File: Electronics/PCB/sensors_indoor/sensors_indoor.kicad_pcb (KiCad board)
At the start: 4 copper layers, 50 x 50 mm, 61 parts, among them J1 USB4125-GF-A, J2 STDC14, J3 B5B-ZR, Q1 DMN62D0U, SW1 SW_Push, U1 MIC5219-3.3YM5, U10 SPS30, U11 74LVC1G08, U2 STM32WBA5MMG, U3 FM24CL16B, U4 LPS22DF, U5 SHT45-AD1F, U6 SCD41-D-R2, U7 SGP41, U8 OPT4001DTSR, U9 TSOP38436

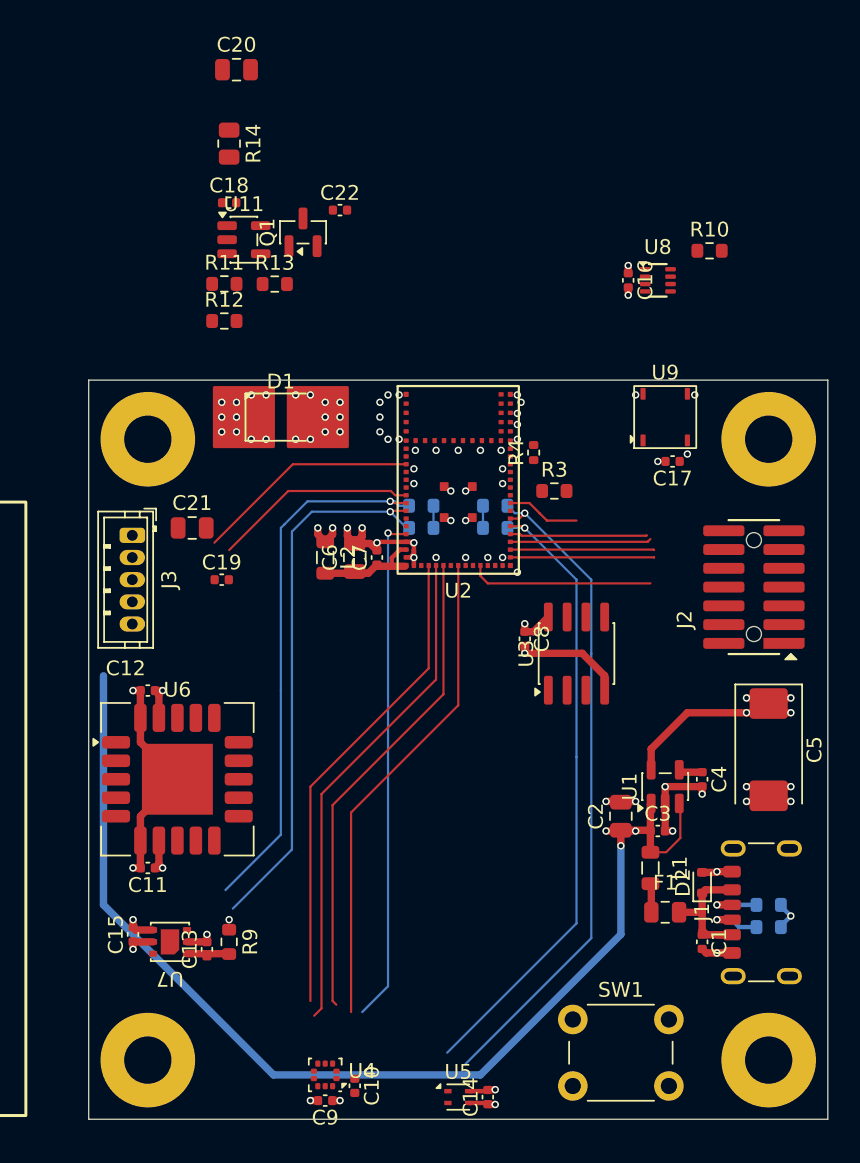
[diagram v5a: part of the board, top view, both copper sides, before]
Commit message: Completed schematic, done most routing
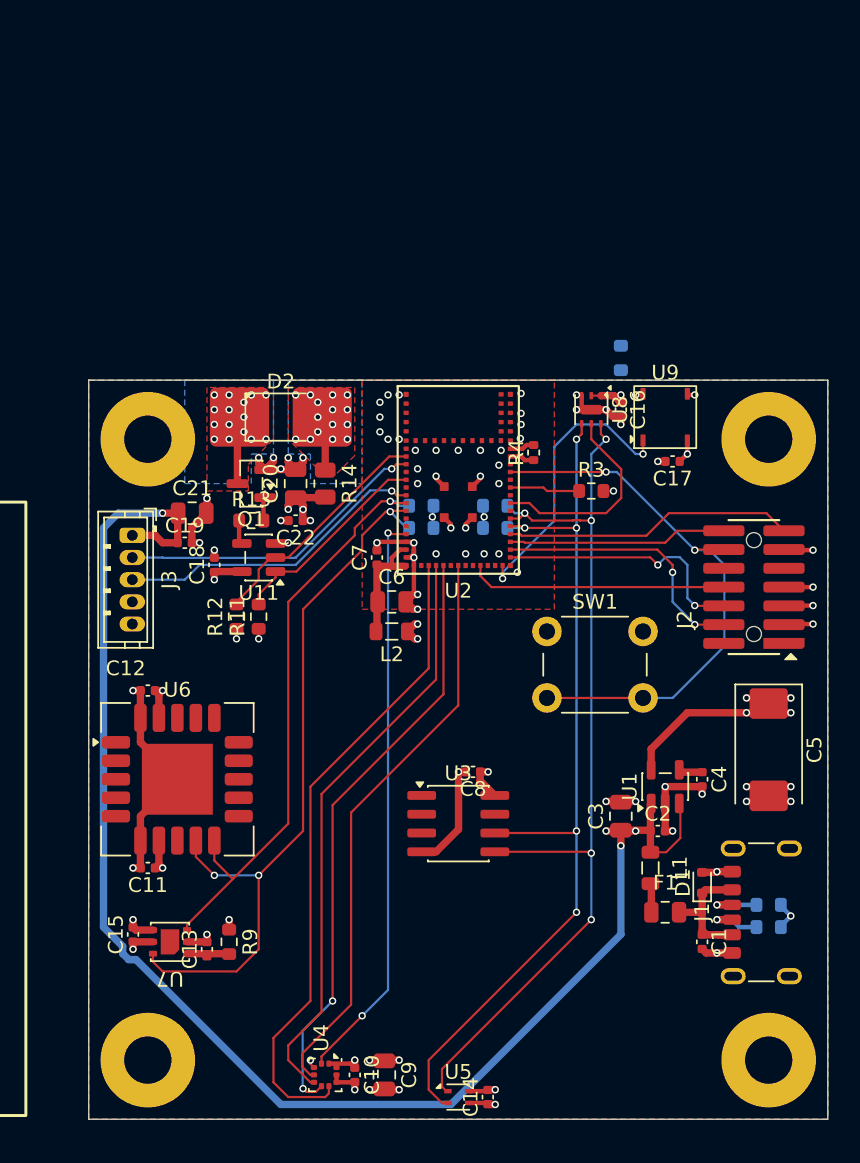
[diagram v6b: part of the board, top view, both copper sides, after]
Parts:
- C9: value 0.1u -> 4.7u; footprint Capacitor_SMD:C_0402_1005Metric -> Capacitor_SMD:C_0805_2012Metric
- R10: moved to B.Cu
- U8: value OPT4001DTSR -> OPT4001DNPRQ1; footprint DWlib:TI_SOT-5X3_OPT4001DTSR -> DWlib:TI_USON-6-1EP_2x2mm_P0.5mm_EP0.65x1.35mm
- moved C20 28.3 mm to (89.0, 82.0), turned to 90 degrees
- moved SW1 26.3 mm to (106.0, 92.0)
- moved C18 24.5 mm to (83.5, 87.5), turned to 90 degrees
- moved R14 23.9 mm to (91.0, 82.0)
- moved R11 22.6 mm to (86.5, 91.0), turned to 90 degrees
- moved U11 21.5 mm to (86.5, 87.0), turned to 180 degrees
- moved C22 21.2 mm to (89.0, 84.5), turned to 180 degrees
- moved R12 20.0 mm to (85.0, 91.0), turned to 90 degrees
- moved Q1 17.4 mm to (86.0, 82.0), turned to 180 degrees
- moved R13 16.1 mm to (86.0, 84.5)
- moved U3 14.0 mm to (100.0, 105.0), turned to 0 degrees
- moved U8 9.84 mm to (109.0, 77.0), turned to -90 degrees
- moved C8 9.66 mm to (101.0, 101.5), turned to 180 degrees
- moved R10 9.41 mm to (111.0, 73.5), turned to -90 degrees
- moved C16 8.76 mm to (111.0, 77.0)
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- renumbered C3 to C2, C2 to C3, D2 to D1, D1 to D2
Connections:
- R11 pad 2: IR_CARRIER -> IR_OUT
- R12 pad 2: IR_OUT -> IR_CARRIER
- U11 pad 1: IR_CARRIER -> IR_OUT
- U11 pad 2: IR_OUT -> IR_CARRIER
- U8 pad 3: unconnected-(U8-NC-Pad3) -> GND
- U8 pad 4: GND -> I2C1_SCL
- U8 pad 5: I2C1_SCL -> INT_ALS
- U8 pad 6: unconnected-(U8-NC-Pad6) -> I2C1_SDA
- U8 pad 7: INT_ALS -> GND
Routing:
- net /indoor_MCU/NRST: track 0.00 -> 38.0 mm, vias 0 -> 2
- net GND: track 59.7 -> 95.1 mm, vias 58 -> 79
- net +5V: track 78.4 -> 102.0 mm, vias 3 -> 4
- net IR_IN: track 0.00 -> 19.7 mm, vias 0 -> 2
- net I2C1_SCL: track 42.8 -> 62.3 mm, vias 1 -> 5
- net I2C1_SDA: track 45.1 -> 63.9 mm, vias 1 -> 5
- net +3.3V: track 32.4 -> 50.0 mm, vias 15 -> 24
- net IR_CARRIER: track 0.00 -> 16.1 mm
- net IR_OUT: track 0.00 -> 14.1 mm
- net I2C3_SCL: track 37.2 -> 50.8 mm, vias 1 -> 3
- net INT_PRES: track 32.8 -> 44.1 mm
- net /indoor_MCU/VCP_RX: track 9.28 -> 19.7 mm
- net INT_ALS: track 4.97 -> 14.1 mm
- net /indoor_MCU/SWDIO: track 9.74 -> 18.0 mm, vias 0 -> 2
- net SPI_CS: track 32.9 -> 40.8 mm, vias 0 -> 2
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- added copper zone on B.Cu, net GND
- added copper zone on F.Cu, net GND
- added copper zone on B.Cu, net Net-(D2-A)
- added copper zone on F.Cu, net Net-(D2-A)
- added copper zone on B.Cu, net Net-(D2-K)
- added copper zone on F.Cu, net Net-(D2-K)

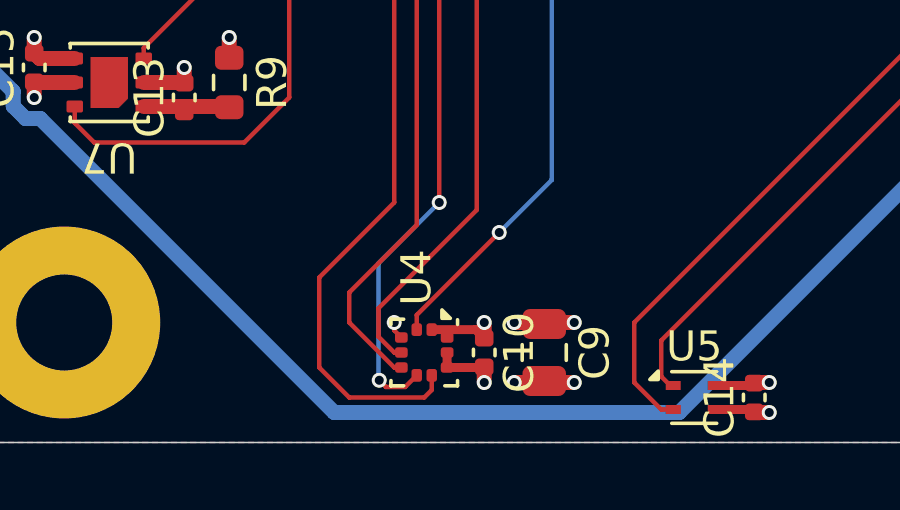
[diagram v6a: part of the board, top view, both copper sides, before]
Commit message: Improved pressure sensor footprint
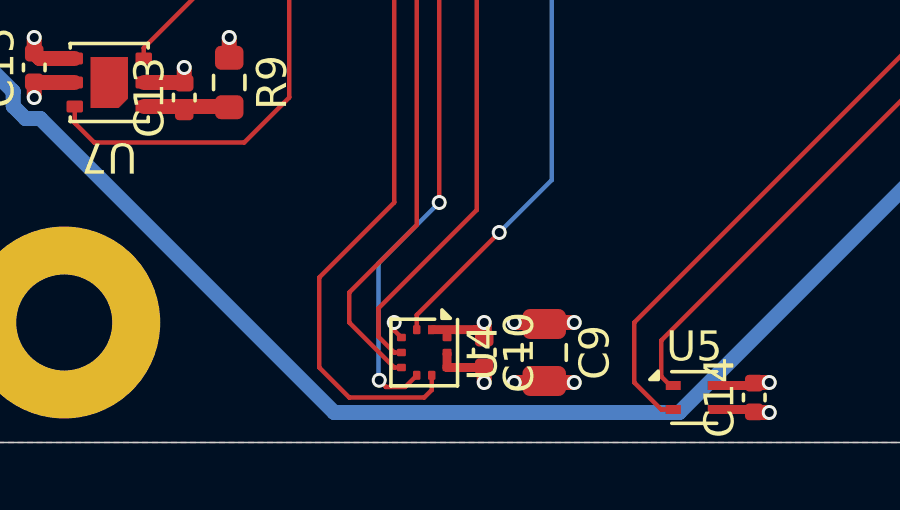
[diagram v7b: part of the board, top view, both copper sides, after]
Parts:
- U4: footprint Package_LGA:ST_HLGA-10_2x2mm_P0.5mm_LayoutBorder3x2y -> DWlib:ST_HLGA-10L_2x2mm_P0.5mm_LayoutBorder3x2y
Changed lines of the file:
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@@
 		)
 	)
-	(footprint "Package_LGA:ST_HLGA-10_2x2mm_P0.5mm_LayoutBorder3x2y"
+	(footprint "DWlib:ST_HLGA-10L_2x2mm_P0.5mm_LayoutBorder3x2y"
 		(layer "F.Cu")
 		(at 91 122 -90)
-		(descr "ST  HLGA, 10 Pin (https://www.st.com/resource/en/datasheet/lps22hh.pdf#page=55), generated with kicad-footprint-generator ipc_noLead_generator.py")
+		(descr "ST  HLGA, 10 Pin (https://www.st.com/resource/en/datasheet/lps22df.pdf#page=44)")
 		(tags "ST HLGA NoLead")
 		(property "Reference" "U4"
-			(at -2.5 0.2625 90)
+			(at 0 -1.95 270)
 			(layer "F.SilkS")
 			(effects
@@
 		)
 		(property "Value" "LPS22DF"
-			(at 0 1.95 90)
+			(at 0 1.95 270)
 			(layer "F.Fab")
 			(effects
@@
 		)
 		(property "Datasheet" "https://www.st.com/resource/en/datasheet/lps22df.pdf"
-			(at 0 0 90)
+			(at 0 0 270)
 			(layer "F.Fab")
 			(hide yes)
@@
 		)
 		(property "Description" "MEMS absolute pressure sensor, 260-1260 hPa, 1-200Hz ODR, 24bit, I2C/I3C/SPI interface, 2x2mm ST_HLGA-10L"
-			(at 0 0 90)
+			(at 0 0 270)
 			(layer "F.Fab")
 			(hide yes)
@@
 		(fp_line
 			(start -1.11 1.11)
-			(end -1.11 0.685)
-			(stroke
-				(width 0.12)
-				(type solid)
-			)
-			(layer "F.SilkS")
-		)
-		(fp_line
-			(start -0.935 1.11)
-			(end -1.11 1.11)
+			(end -1.11 -0.35)
 			(stroke
 				(width 0.12)
@@
 		(fp_line
 			(start 1.11 1.11)
-			(end 0.935 1.11)
-			(stroke
-				(width 0.12)
-				(type solid)
-			)
-			(layer "F.SilkS")
-		)
-		(fp_line
-			(start 1.11 0.685)
-			(end 1.11 1.11)
-			(stroke
-				(width 0.12)
-				(type solid)
-			)
-			(layer "F.SilkS")
-		)
-		(fp_line
-			(start -1.092261 -1.11)
-			(end -0.935 -1.11)
+			(end -1.11 1.11)
 			(stroke
 				(width 0.12)
@@
 		)
 		(fp_line
-			(start 0.935 -1.11)
+			(start -1.1 -1.11)
 			(end 1.11 -1.11)
 			(stroke
@@
 		(fp_line
 			(start 1.11 -1.11)
-			(end 1.11 -0.685)
+			(end 1.11 1.11)
 			(stroke
 				(width 0.12)
@@
 		)
 		(fp_text user "${REFERENCE}"
-			(at 0 0 90)
+			(at 0 0 270)
 			(layer "F.Fab")
 			(effects
@@
 		)
 		(pad "1" smd roundrect
-			(at -0.7625 -0.25 270)
-			(size 0.425 0.35)
+			(at -0.76 -0.25 270)
+			(size 0.3 0.25)
 			(layers "F.Cu" "F.Mask" "F.Paste")
-			(roundrect_rratio 0.25)
+			(roundrect_rratio 0.15)
+			(chamfer_ratio 0.2)
+			(chamfer top_right)
 			(net 2 "+3.3V")
 			(pinfunction "Vdd_IO")
@@
 		)
 		(pad "2" smd roundrect
-			(at -0.7625 0.25 270)
-			(size 0.425 0.35)
+			(at -0.76 0.25 270)
+			(size 0.3 0.25)
 			(layers "F.Cu" "F.Mask" "F.Paste")
-			(roundrect_rratio 0.25)
+			(roundrect_rratio 0.15)
 			(net 13 "SPI_SCLK")
 			(pinfunction "SCL")
@@
 		)
 		(pad "3" smd roundrect
-			(at -0.5 0.7625 270)
-			(size 0.35 0.425)
+			(at -0.5 0.76)
+			(size 0.3 0.25)
 			(layers "F.Cu" "F.Mask" "F.Paste")
-			(roundrect_rratio 0.25)
+			(roundrect_rratio 0.15)
 			(net 3 "GND")
 			(pinfunction "GND")
@@
 		)
 		(pad "4" smd roundrect
-			(at 0 0.7625 270)
-			(size 0.35 0.425)
+			(at 0 0.76)
+			(size 0.3 0.25)
 			(layers "F.Cu" "F.Mask" "F.Paste")
-			(roundrect_rratio 0.25)
+			(roundrect_rratio 0.15)
 			(net 14 "SPI_MOSI")
 			(pinfunction "SDI")
@@
 		)
 		(pad "5" smd roundrect
-			(at 0.5 0.7625 270)
-			(size 0.35 0.425)
+			(at 0.5 0.76)
+			(size 0.3 0.25)
 			(layers "F.Cu" "F.Mask" "F.Paste")
-			(roundrect_rratio 0.25)
+			(roundrect_rratio 0.15)
 			(net 12 "SPI_MISO")
 			(pinfunction "SDO")
@@
 		)
 		(pad "6" smd roundrect
-			(at 0.7625 0.25 270)
-			(size 0.425 0.35)
+			(at 0.76 0.25 270)
+			(size 0.3 0.25)
 			(layers "F.Cu" "F.Mask" "F.Paste")
-			(roundrect_rratio 0.25)
+			(roundrect_rratio 0.15)
 			(net 11 "SPI_CS")
 			(pinfunction "~{CS}")
@@
 		)
 		(pad "7" smd roundrect
-			(at 0.7625 -0.25 270)
-			(size 0.425 0.35)
+			(at 0.76 -0.25 270)
+			(size 0.3 0.25)
 			(layers "F.Cu" "F.Mask" "F.Paste")
-			(roundrect_rratio 0.25)
+			(roundrect_rratio 0.15)
 			(net 32 "INT_PRES")
 			(pinfunction "INT_DRDY")
@@
 		)
 		(pad "8" smd roundrect
-			(at 0.5 -0.7625 270)
-			(size 0.35 0.425)
+			(at 0.5 -0.76)
+			(size 0.3 0.25)
 			(layers "F.Cu" "F.Mask" "F.Paste")
-			(roundrect_rratio 0.25)
+			(roundrect_rratio 0.15)
 			(net 3 "GND")
 			(pinfunction "GND_IO")
@@
 		)
 		(pad "9" smd roundrect
-			(at 0 -0.7625 270)
-			(size 0.35 0.425)
+			(at 0 -0.76)
+			(size 0.3 0.25)
 			(layers "F.Cu" "F.Mask" "F.Paste")
-			(roundrect_rratio 0.25)
+			(roundrect_rratio 0.15)
 			(net 3 "GND")
 			(pinfunction "GND")
@@
 		)
 		(pad "10" smd roundrect
-			(at -0.5 -0.7625 270)
-			(size 0.35 0.425)
+			(at -0.5 -0.76)
+			(size 0.3 0.25)
 			(layers "F.Cu" "F.Mask" "F.Paste")
-			(roundrect_rratio 0.25)
+			(roundrect_rratio 0.15)
 			(net 2 "+3.3V")
 			(pinfunction "VDD")
@@
 		(min_thickness 0.25)
 		(filled_areas_thickness no)
-		(fill yes
+		(fill
 			(thermal_gap 0.5)
 			(thermal_bridge_width 0.5)
@@
 		(min_thickness 0.15)
 		(filled_areas_thickness no)
-		(fill yes
+		(fill
 			(thermal_gap 0.3)
 			(thermal_bridge_width 0.3)
@@
 		(min_thickness 0.25)
 		(filled_areas_thickness no)
-		(fill yes
+		(fill
 			(thermal_gap 0.5)
 			(thermal_bridge_width 0.5)
@@
 		(min_thickness 0.2)
 		(filled_areas_thickness no)
-		(fill yes
+		(fill
 			(thermal_gap 0.3)
 			(thermal_bridge_width 0.3)
@@
 		(min_thickness 0.2)
 		(filled_areas_thickness no)
-		(fill yes
+		(fill
 			(thermal_gap 0.5)
 			(thermal_bridge_width 0.5)
@@
 		(min_thickness 0.2)
 		(filled_areas_thickness no)
-		(fill yes
+		(fill
 			(thermal_gap 0.5)
 			(thermal_bridge_width 0.5)
@@
 		(min_thickness 0.25)
 		(filled_areas_thickness no)
-		(fill yes
+		(fill
 			(thermal_gap 0.3)
 			(thermal_bridge_width 0.3)
@@
 		(min_thickness 0.25)
 		(filled_areas_thickness no)
-		(fill yes
+		(fill
 			(thermal_gap 0.3)
 			(thermal_bridge_width 0.3)

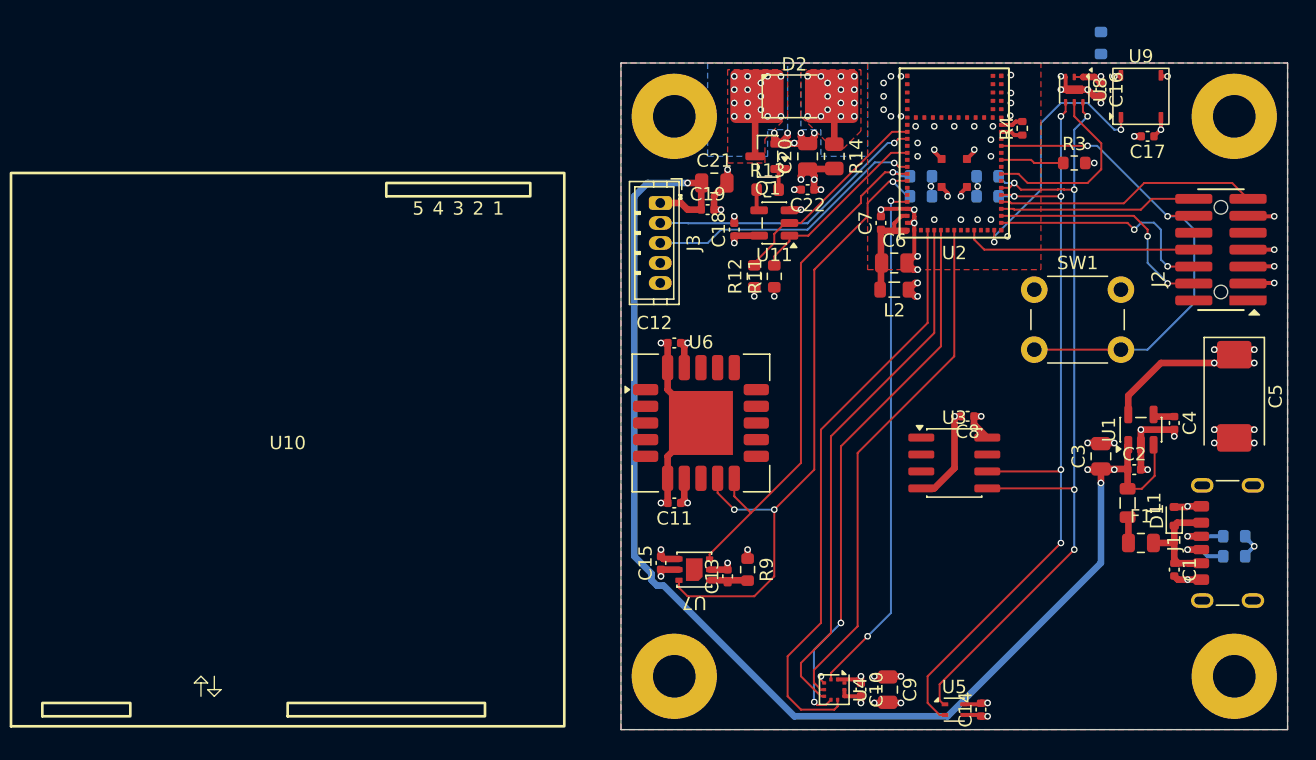
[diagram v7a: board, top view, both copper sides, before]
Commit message: Placed designators on PCB
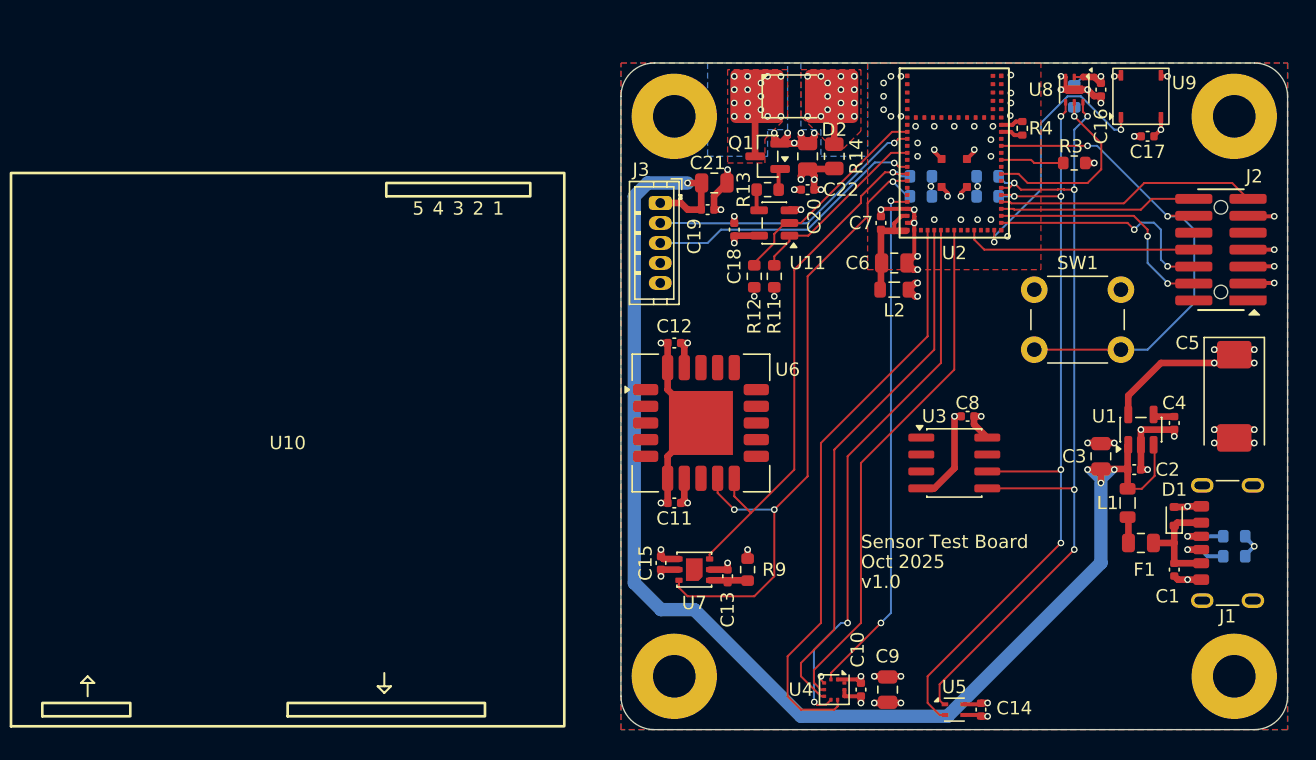
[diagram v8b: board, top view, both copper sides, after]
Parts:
- moved R10 4.47 mm to (109.0, 77.5), turned to 90 degrees
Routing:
- net +5V: track 102.0 -> 104.7 mm
- net +3.3V: track 50.0 -> 52.2 mm
- net /VBUS: track 9.34 -> 8.51 mm
- net INT_ALS: track 14.1 -> 14.7 mm, vias 0 -> 1
- net GND: track 95.1 -> 95.7 mm
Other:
- outline, holes or cut-outs redrawn
- board text added: "Oct 2025"
- board text added: "Sensor Test Board"
- board text added: "v1.0"
